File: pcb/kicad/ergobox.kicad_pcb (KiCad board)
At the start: 2 copper layers, 236 x 147 mm, 79 parts, among them SW1 SW_Push, SW10 Kailh, SW11 Kailh, SW12 Kailh, SW13 Kailh, SW14 Kailh, SW15 Kailh, SW16 Kailh, SW17 Kailh, SW18 Kailh, SW19 Kailh, SW2 SW_Push, SW20 Kailh, SW3 SW_Push, SW4 SW_Push, SW5 SW_Push, SW6 SW_Push, SW7 SW_Push, SW8 SW_Push, SW9 Kailh, U1 TLV73333PDBV, U2 RP2040, U3 W25Q128JVS, Y1 Crystal_GND24

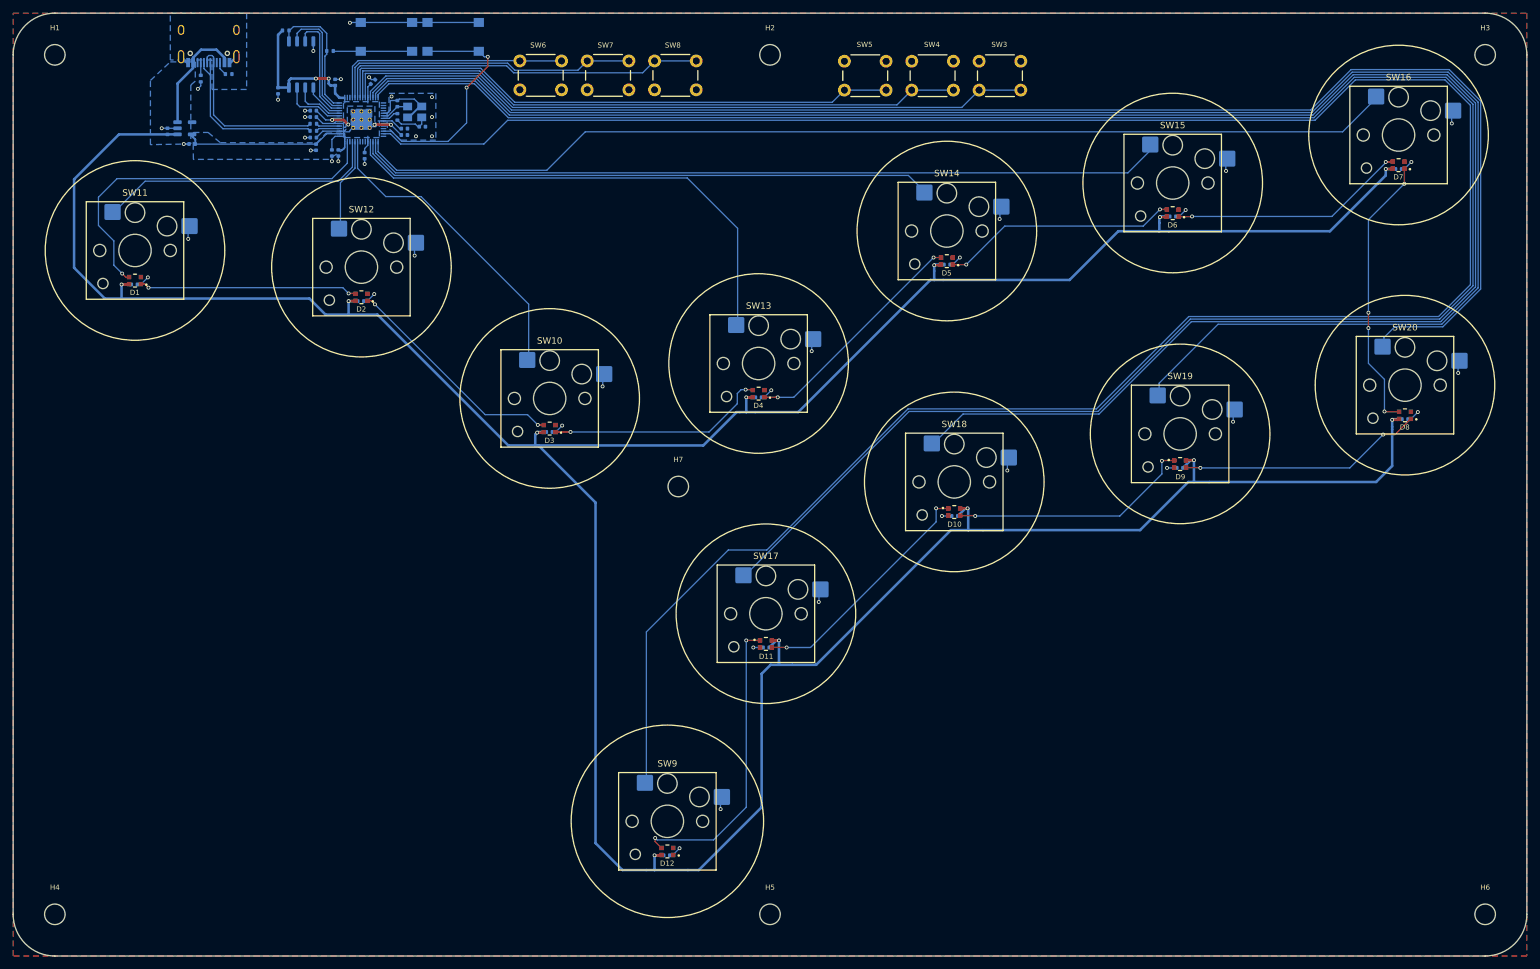
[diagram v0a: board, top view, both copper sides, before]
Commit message: chore: adds silkscreen labels for aux buttons
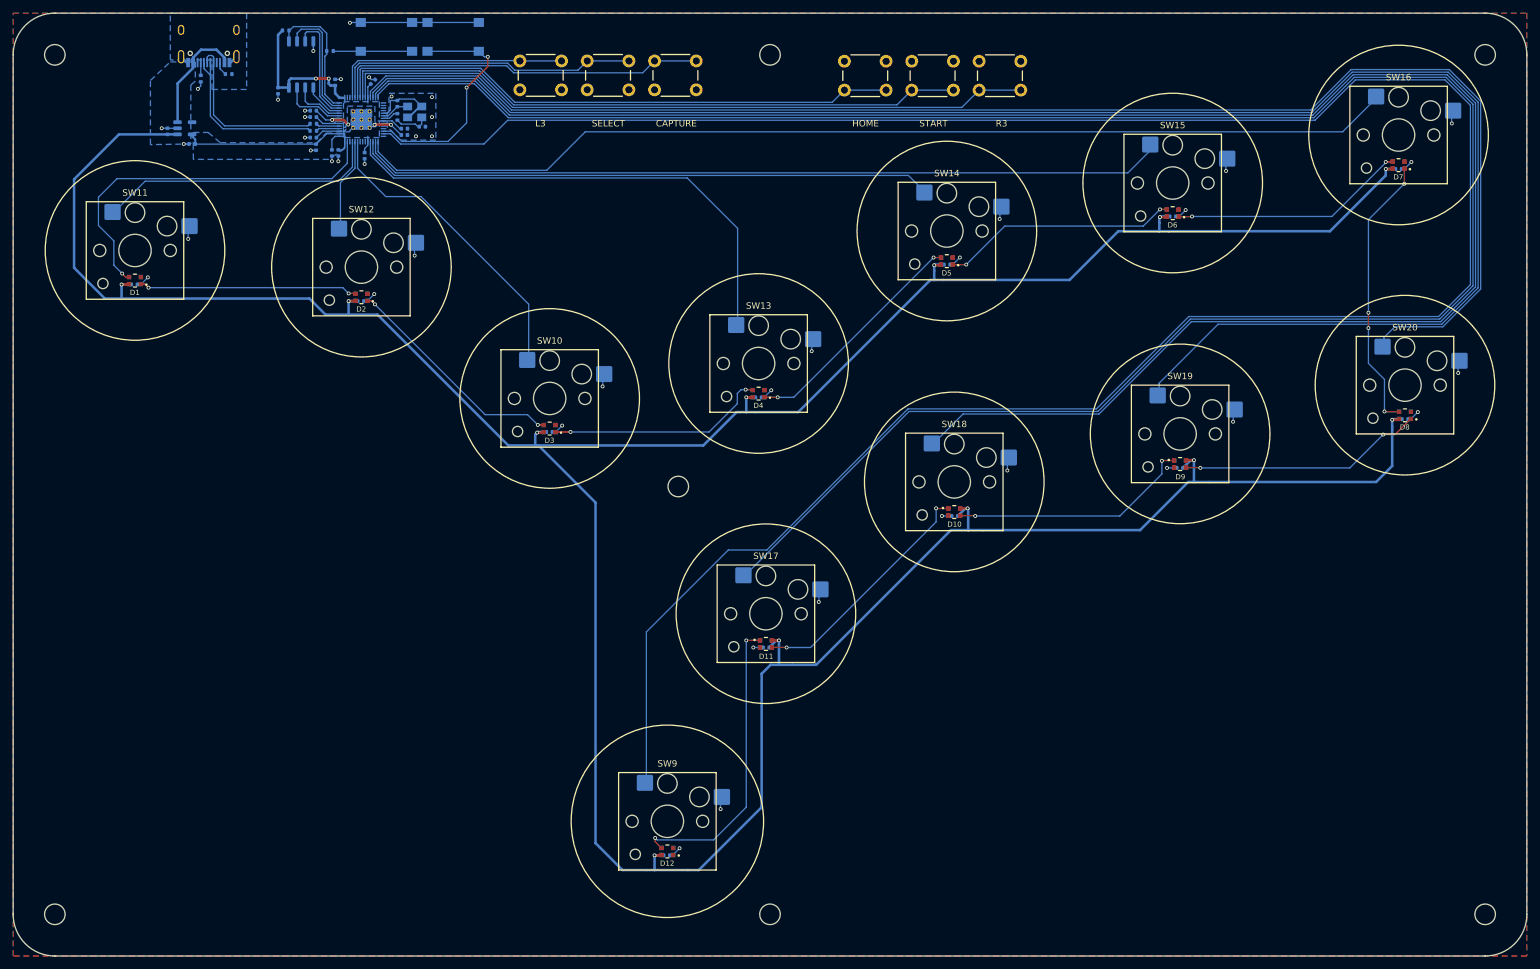
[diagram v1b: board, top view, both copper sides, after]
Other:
- board text added: "CAPTURE"
- board text added: "HOME"
- board text added: "L3"
- board text added: "R3"
- board text added: "SELECT"
- board text added: "START"
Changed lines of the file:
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@@
     (property "Sheetname" "")
     (attr through_hole)
-    (fp_text reference "SW4" (at 3.35 7.1) (layer "F.SilkS")
+    (fp_text reference "SW4" (at 3.35 7.1) (layer "F.SilkS") hide
       (effects (font (size 0.8 0.8) (thickness 0.15)))
     )
@@
     (property "Sheetname" "")
     (attr through_hole)
-    (fp_text reference "SW5" (at 3.35 7.1) (layer "F.SilkS")
+    (fp_text reference "SW5" (at 3.35 7.1) (layer "F.SilkS") hide
       (effects (font (size 0.8 0.8) (thickness 0.15)))
     )
@@
     (property "Sheetname" "")
     (attr exclude_from_pos_files)
-    (fp_text reference "H7" (at 0 -4.2) (layer "F.SilkS")
+    (fp_text reference "H7" (at 0 -4.2) (layer "F.SilkS") hide
       (effects (font (size 0.8 0.8) (thickness 0.15)))
     )
@@
     (property "Sheetname" "")
     (attr exclude_from_pos_files)
-    (fp_text reference "H5" (at 0 -4.2) (layer "F.SilkS")
+    (fp_text reference "H5" (at 0 -4.2) (layer "F.SilkS") hide
       (effects (font (size 0.8 0.8) (thickness 0.15)))
     )
@@
     (property "Sheetname" "")
     (attr exclude_from_pos_files)
-    (fp_text reference "H2" (at 0 -4.2) (layer "F.SilkS")
+    (fp_text reference "H2" (at 0 -4.2) (layer "F.SilkS") hide
       (effects (font (size 0.8 0.8) (thickness 0.15)))
     )
@@
     (property "Sheetname" "")
     (attr exclude_from_pos_files)
-    (fp_text reference "H4" (at 0 -4.2) (layer "F.SilkS")
+    (fp_text reference "H4" (at 0 -4.2) (layer "F.SilkS") hide
       (effects (font (size 0.8 0.8) (thickness 0.15)))
     )
@@
     (property "Sheetname" "")
     (attr through_hole)
-    (fp_text reference "SW7" (at 2.85 -2.45) (layer "F.SilkS")
+    (fp_text reference "SW7" (at 2.85 -2.45) (layer "F.SilkS") hide
       (effects (font (size 0.8 0.8) (thickness 0.15)))
     )
@@
     (property "Sheetname" "")
     (attr through_hole)
-    (fp_text reference "SW3" (at 3.35 7.1) (layer "F.SilkS")
+    (fp_text reference "SW3" (at 3.35 7.1) (layer "F.SilkS") hide
       (effects (font (size 0.8 0.8) (thickness 0.15)))
     )
@@
     (property "Sheetname" "")
     (attr exclude_from_pos_files)
-    (fp_text reference "H6" (at 0 -4.2) (layer "F.SilkS")
+    (fp_text reference "H6" (at 0 -4.2) (layer "F.SilkS") hide
       (effects (font (size 0.8 0.8) (thickness 0.15)))
     )
@@
     (property "Sheetname" "")
     (attr exclude_from_pos_files)
-    (fp_text reference "H3" (at 0 -4.2) (layer "F.SilkS")
+    (fp_text reference "H3" (at 0 -4.2) (layer "F.SilkS") hide
       (effects (font (size 0.8 0.8) (thickness 0.15)))
     )
@@
     (property "Sheetname" "")
     (attr exclude_from_pos_files)
-    (fp_text reference "H1" (at 0 -4.2) (layer "F.SilkS")
+    (fp_text reference "H1" (at 0 -4.2) (layer "F.SilkS") hide
       (effects (font (size 0.8 0.8) (thickness 0.15)))
     )
@@
     (property "Sheetname" "")
     (attr through_hole)
-    (fp_text reference "SW8" (at 2.85 -2.45) (layer "F.SilkS")
+    (fp_text reference "SW8" (at 2.85 -2.45) (layer "F.SilkS") hide
       (effects (font (size 0.8 0.8) (thickness 0.15)))
     )
@@
     (property "Sheetname" "")
     (attr through_hole)
-    (fp_text reference "SW6" (at 2.85 -2.45) (layer "F.SilkS")
+    (fp_text reference "SW6" (at 2.85 -2.45) (layer "F.SilkS") hide
       (effects (font (size 0.8 0.8) (thickness 0.15)))
     )
@@
   (gr_arc locked (start 67.8 200.3) (mid 63.203806 198.396194) (end 61.3 193.8) (layer "Edge.Cuts") (width 0.1))
   (gr_arc locked (start 297.3 193.8) (mid 295.396194 198.396194) (end 290.8 200.3) (layer "Edge.Cuts") (width 0.1))
+  (gr_text "R3" (at 215.4 70.5) (layer "F.SilkS")
+    (effects (font (size 1 1) (thickness 0.15)))
+  )
+  (gr_text "HOME" (at 194.2 70.5) (layer "F.SilkS")
+    (effects (font (size 1 1) (thickness 0.15)))
+  )
+  (gr_text "SELECT" (at 154.1 70.5) (layer "F.SilkS")
+    (effects (font (size 1 1) (thickness 0.15)))
+  )
+  (gr_text "CAPTURE" (at 164.7 70.5) (layer "F.SilkS")
+    (effects (font (size 1 1) (thickness 0.15)))
+  )
+  (gr_text "START" (at 204.8 70.5) (layer "F.SilkS")
+    (effects (font (size 1 1) (thickness 0.15)))
+  )
+  (gr_text "L3" (at 143.5 70.5) (layer "F.SilkS")
+    (effects (font (size 1 1) (thickness 0.15)))
+  )
   (segment (start 112.828851 69.9505) (end 113.5505 70.672149) (width 0.4) (layer "F.Cu") (net 1))
   (segment (start 120.2 70.7) (end 117.6495 70.7) (width 0.4) (layer "F.Cu") (net 1))

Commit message: chore: adds GPIO pin numbers for button assignments to B.Silkscreen
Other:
- board text added: "04 L3 09 R3 08 START 05 SELECT 07 HOME 06 CAPTURE"
- board text added: "39 LEFT 38 DOWN 37 RIGHT 36 UP 32 P1 31 P2 30 P3 29 P4 14 K1 13 K2 12 K3 11 K4"
- board text added: "ver 0.2.20200930"
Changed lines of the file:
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@@
     )
   )
+  (gr_line (start 126.1 150.9) (end 126.1 141.9) (layer "B.SilkS") (width 0.3))
+  (gr_line (start 126.1 141.9) (end 117.1 141.9) (layer "B.SilkS") (width 0.3))
   (gr_circle (center 178.66283 146.938858) (end 192.66283 146.938858) (layer "F.SilkS") (width 0.2) (fill none))
   (gr_circle (center 278.3 111.3) (end 292.3 111.3) (layer "F.SilkS") (width 0.2) (fill none))
@@
   (gr_arc locked (start 67.8 200.3) (mid 63.203806 198.396194) (end 61.3 193.8) (layer "Edge.Cuts") (width 0.1))
   (gr_arc locked (start 297.3 193.8) (mid 295.396194 198.396194) (end 290.8 200.3) (layer "Edge.Cuts") (width 0.1))
+  (gr_text "39  LEFT\n38  DOWN\n37  RIGHT\n36  UP\n\n32  P1\n31  P2\n30  P3\n29  P4\n\n14  K1\n13  K2\n12  K3\n11  K4\n\n" (at 123.3 168.9) (layer "B.SilkS")
+    (effects (font (size 2 2) (thickness 0.25)) (justify left mirror))
+  )
+  (gr_text "ver 0.2.20200930" (at 68.2 172 90) (layer "B.SilkS")
+    (effects (font (size 2 2) (thickness 0.15)) (justify mirror))
+  )
+  (gr_text "04  L3\n09  R3\n\n08  START\n05  SELECT\n07  HOME\n06  CAPTURE" (at 102.3 178.6) (layer "B.SilkS")
+    (effects (font (size 2 2) (thickness 0.25)) (justify left mirror))
+  )
   (gr_text "R3" (at 215.4 70.5) (layer "F.SilkS")
     (effects (font (size 1 1) (thickness 0.15)))

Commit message: fix: adds LED data GPIO pin to B.Silkscreen legend
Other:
- board text added: "41 LED 04 L3 09 R3 08 START 05 SELECT 07 HOME 06 CAPTURE"
- board text removed: "04 L3 09 R3 08 START 05 SELECT 07 HOME 06 CAPTURE"
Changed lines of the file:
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@@
     (effects (font (size 2 2) (thickness 0.15)) (justify mirror))
   )
-  (gr_text "04  L3\n09  R3\n\n08  START\n05  SELECT\n07  HOME\n06  CAPTURE" (at 102.3 178.6) (layer "B.SilkS")
+  (gr_text "41  LED\n\n04  L3\n09  R3\n\n08  START\n05  SELECT\n07  HOME\n06  CAPTURE" (at 102.8 175.4) (layer "B.SilkS")
     (effects (font (size 2 2) (thickness 0.25)) (justify left mirror))
   )
